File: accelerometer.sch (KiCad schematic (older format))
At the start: 10 parts, among them U301 PCA9306, U302 ICM-20948

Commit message: PMD03 - Creacion PCB y modelo 3D
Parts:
- U302: footprint Sensor_Motion:InvenSense_QFN-24_3x3mm_P0.4mm_NoMask -> Sensor_Motion:InvenSense_QFN-24_3x3mm_P0.4mm
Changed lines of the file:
@@
 F 0 "U302" H 7150 3050 50  0000 C CNN
 F 1 "ICM-20948" H 7750 3050 50  0000 C CNN
-F 2 "Sensor_Motion:InvenSense_QFN-24_3x3mm_P0.4mm_NoMask" H 7500 2700 50  0001 C CNN
+F 2 "Sensor_Motion:InvenSense_QFN-24_3x3mm_P0.4mm" H 7500 2700 50  0001 C CNN
 F 3 "http://www.invensense.com/wp-content/uploads/2016/06/DS-000189-ICM-20948-v1.3.pdf" H 7500 3550 50  0001 C CNN
 	1    7500 3700

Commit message: Correcciones
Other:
- note added: "Manufacturer TDK InvenSense \nMfr. Part # ICM-20948 \nMouser Part # 410-ICM-20948 \nPackage # 24-Pin QFN\n\nAlternativa (No recomendada):\n\nManufacturer TDK InvenSense \nMfr. Part # MPU-9250 \nMouser Part # 410-MPU-9250 \nPackage # 24-Pin QFN"
- note added: "Manufacturer Texas Instruments \nMfr. Part # PCA9306DCUR \nMouser Part # 595-PCA9306DCUR \nPackage # VSSOP-8"
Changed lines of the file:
@@
 Title "Replica ESP32 Thing - Inertial measurement unit"
 Date ""
-Rev "Piza AG"
-Comp "Facundo A Lucianna"
+Rev "1.1"
+Comp "Autor: Facundo A Lucianna - Revisor: Alvaro Gabriel Pizá"
 Comment1 "Modificacion: Agregado de IMU"
 Comment2 "https://creativecommons.org/licenses/by-sa/4.0/"
@@
 Wire Wire Line
 	6900 3400 7000 3400
+Text Notes 5050 4350 0    50   ~ 0
+Manufacturer Texas Instruments \nMfr. Part # PCA9306DCUR \nMouser Part # 595-PCA9306DCUR \nPackage # VSSOP-8
+Text Notes 8400 3950 0    50   ~ 0
+Manufacturer TDK InvenSense \nMfr. Part # ICM-20948 \nMouser Part # 410-ICM-20948 \nPackage # 24-Pin QFN\n\nAlternativa (No recomendada):\n\nManufacturer TDK InvenSense \nMfr. Part # MPU-9250  \nMouser Part # 410-MPU-9250 \nPackage # 24-Pin QFN
 $EndSCHEMATC

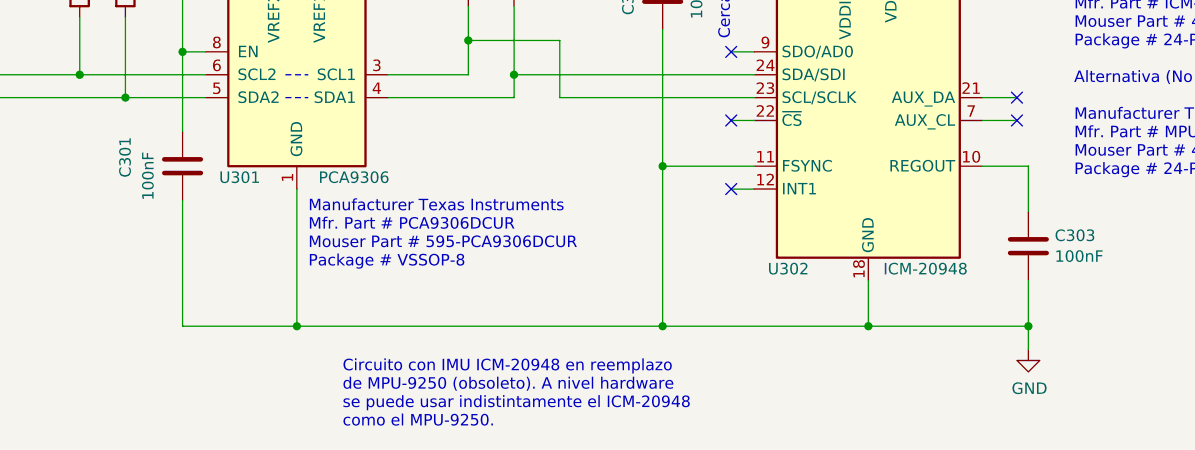
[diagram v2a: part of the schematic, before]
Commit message: Cambio en esquematico
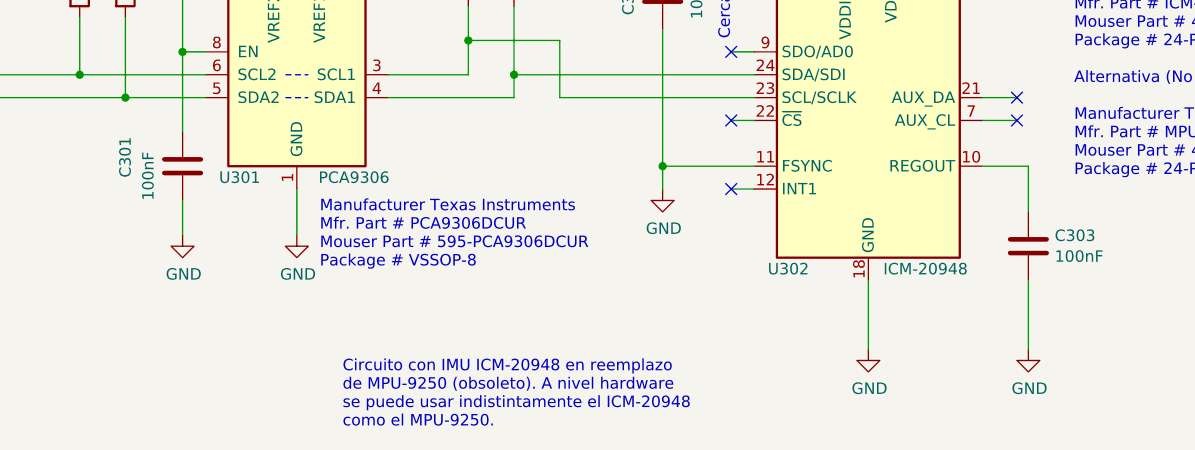
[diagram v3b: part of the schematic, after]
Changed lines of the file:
@@
 $EndComp
-Wire Wire Line
-	6600 4600 7500 4600
-Connection ~ 7500 4600
-Wire Wire Line
-	7500 4600 7500 4400
 Wire Wire Line
 	7000 3900 6600 3900
-Connection ~ 6600 3900
-Wire Wire Line
-	6600 3900 6600 4600
 NoConn ~ 6900 4000
 Wire Wire Line
@@
 Wire Wire Line
 	8200 3900 8200 4100
-Wire Wire Line
-	8200 4400 8200 4600
 Text HLabel 5750 2550 1    50   UnSpc ~ 0
 VDD1.8
@@
 Wire Wire Line
 	3700 2750 3700 2650
-Wire Wire Line
-	5000 4600 5000 4000
-Connection ~ 6600 4600
 $Comp
 L Device:C C302
@@
 	4500 3400 4500 3750
 Connection ~ 4500 3400
-Wire Wire Line
-	4500 4050 4500 4600
-Wire Wire Line
-	4500 4600 5000 4600
-Connection ~ 5000 4600
 Wire Notes Line
 	4950 3500 5050 3500
@@
 Wire Wire Line
 	7400 2750 7400 3000
-Wire Wire Line
-	5000 4600 6600 4600
 Text Notes 6900 3350 1    50   ~ 0
 Cerca de Pin 8
@@
 Wire Notes Line
 	3250 3050 3250 4050
-Wire Wire Line
-	8200 4600 7500 4600
-Connection ~ 8200 4600
-Wire Wire Line
-	8200 4600 8200 4700
 $Comp
 L power:PWR_FLAG #FLG0104
@@
 Wire Wire Line
 	6900 3400 7000 3400
-Text Notes 5050 4350 0    50   ~ 0
+Text Notes 5100 4350 0    50   ~ 0
 Manufacturer Texas Instruments \nMfr. Part # PCA9306DCUR \nMouser Part # 595-PCA9306DCUR \nPackage # VSSOP-8
 Text Notes 8400 3950 0    50   ~ 0
 Manufacturer TDK InvenSense \nMfr. Part # ICM-20948 \nMouser Part # 410-ICM-20948 \nPackage # 24-Pin QFN\n\nAlternativa (No recomendada):\n\nManufacturer TDK InvenSense \nMfr. Part # MPU-9250  \nMouser Part # 410-MPU-9250 \nPackage # 24-Pin QFN
+$Comp
+L power:GND #PWR?
+U 1 1 5D14CA9C
+P 7500 4700
+F 0 "#PWR?" H 7500 4450 50  0001 C CNN
+F 1 "GND" H 7505 4527 50  0000 C CNN
+F 2 "" H 7500 4700 50  0001 C CNN
+F 3 "" H 7500 4700 50  0001 C CNN
+	1    7500 4700
+	1    0    0    -1
+$EndComp
+$Comp
+L power:GND #PWR?
+U 1 1 5D14CEA9
+P 6600 4000
+F 0 "#PWR?" H 6600 3750 50  0001 C CNN
+F 1 "GND" H 6605 3827 50  0000 C CNN
+F 2 "" H 6600 4000 50  0001 C CNN
+F 3 "" H 6600 4000 50  0001 C CNN
+	1    6600 4000
+	1    0    0    -1
+$EndComp
+$Comp
+L power:GND #PWR?
+U 1 1 5D14DF88
+P 5000 4200
+F 0 "#PWR?" H 5000 3950 50  0001 C CNN
+F 1 "GND" H 5005 4027 50  0000 C CNN
+F 2 "" H 5000 4200 50  0001 C CNN
+F 3 "" H 5000 4200 50  0001 C CNN
+	1    5000 4200
+	1    0    0    -1
+$EndComp
+$Comp
+L power:GND #PWR?
+U 1 1 5D14E3A8
+P 4500 4200
+F 0 "#PWR?" H 4500 3950 50  0001 C CNN
+F 1 "GND" H 4505 4027 50  0000 C CNN
+F 2 "" H 4500 4200 50  0001 C CNN
+F 3 "" H 4500 4200 50  0001 C CNN
+	1    4500 4200
+	1    0    0    -1
+$EndComp
+Wire Wire Line
+	8200 4400 8200 4700
+Wire Wire Line
+	7500 4400 7500 4700
+Wire Wire Line
+	6600 4000 6600 3900
+Connection ~ 6600 3900
+Wire Wire Line
+	4500 4200 4500 4050
+Wire Wire Line
+	5000 4000 5000 4200
 $EndSCHEMATC
